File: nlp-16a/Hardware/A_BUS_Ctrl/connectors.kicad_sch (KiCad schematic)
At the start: 66 parts, among them J1 Conn_02x20_Odd_Even, J2 Conn_02x10_Counter_Clockwise, J3 Conn_02x10_Counter_Clockwise, J4 Conn_02x10_Counter_Clockwise, J5 Screw_Terminal_01x02

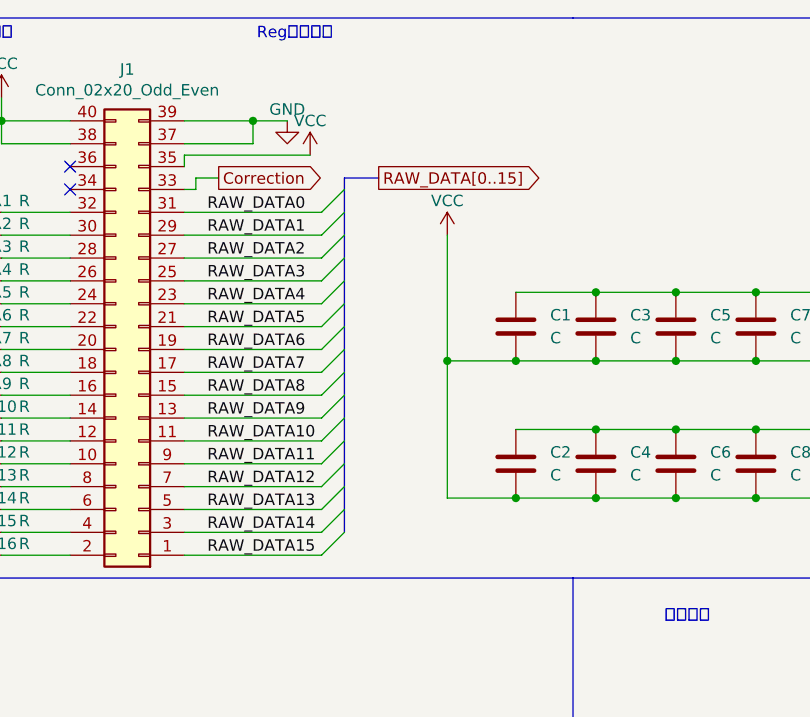
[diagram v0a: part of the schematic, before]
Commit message: テストで見つかった不具合を修正(れジスタアドレスデコーダ，Addrの内部処理の方法を変更)
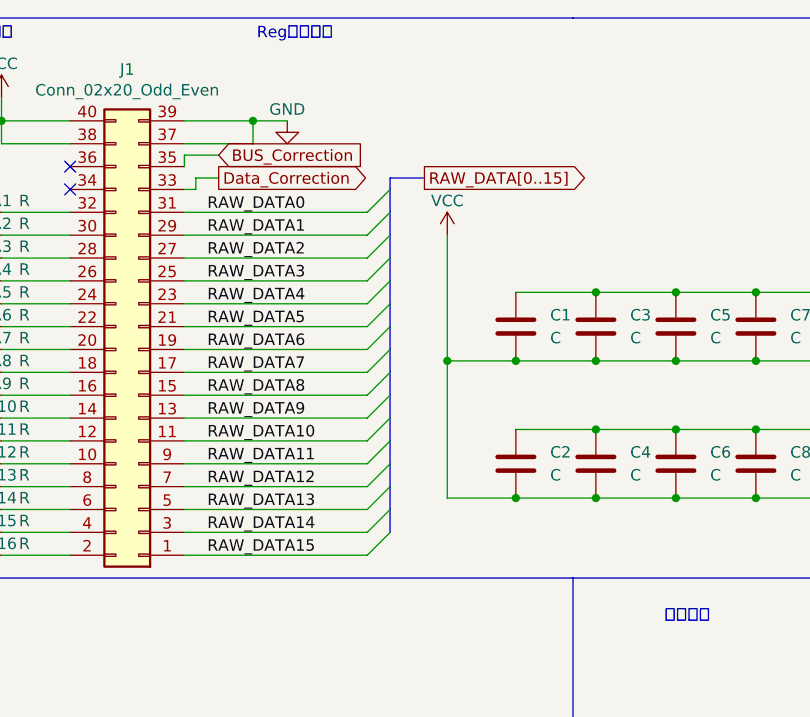
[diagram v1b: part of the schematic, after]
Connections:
- net VCC: no longer J1.35 (Pin_35)
- net Correction renamed Data_Correction
- new net BUS_Correction: J1.35 (Pin_35)

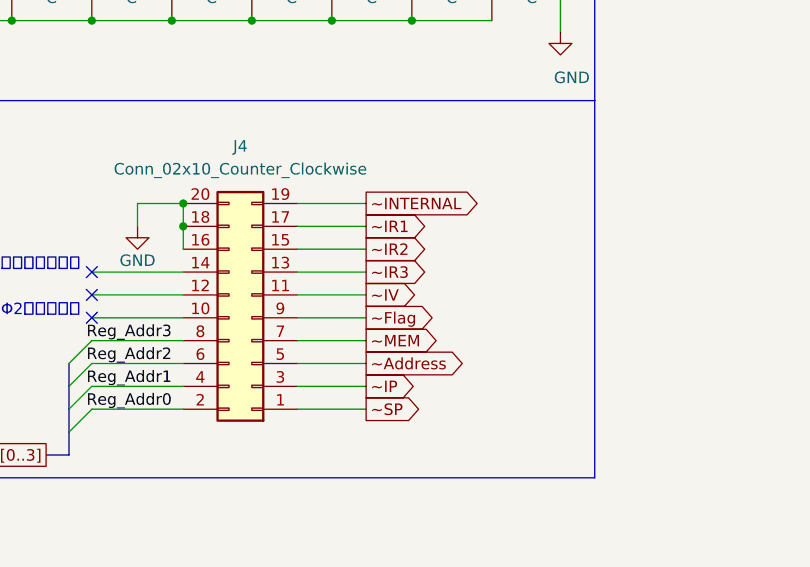
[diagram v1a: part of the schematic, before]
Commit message: A BUS制御 IVとIR3のアドレスの処理変更を反映
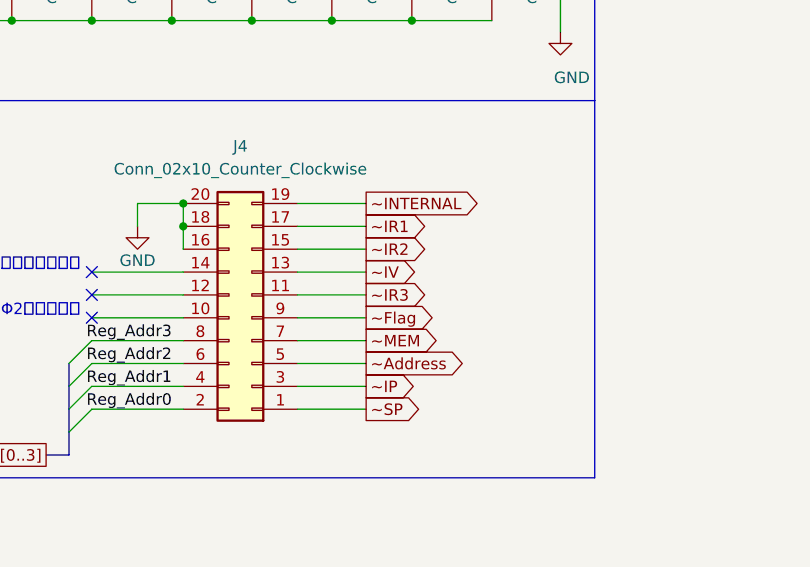
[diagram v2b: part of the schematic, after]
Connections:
- net ~IR3: now also J4.11 (Pin_11); no longer J4.13 (Pin_13)
- net ~IV: now also J4.13 (Pin_13); no longer J4.11 (Pin_11)
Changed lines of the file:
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@@
     )
   )
-  (global_label "~IV" (shape output) (at 251.46 101.6 0) (fields_autoplaced)
+  (global_label "~IV" (shape output) (at 251.46 99.06 0) (fields_autoplaced)
     (effects (font (size 1.27 1.27)) (justify left))
-    (property "Intersheet References" "${INTERSHEET_REFS}" (id 0) (at 256.4736 101.5206 0)
+    (property "Intersheet References" "${INTERSHEET_REFS}" (id 0) (at 256.4736 98.9806 0)
       (effects (font (size 1.27 1.27)) (justify left) hide)
     )
@@
     )
   )
-  (global_label "~IR3" (shape output) (at 251.46 99.06 0) (fields_autoplaced)
+  (global_label "~IR3" (shape output) (at 251.46 101.6 0) (fields_autoplaced)
     (effects (font (size 1.27 1.27)) (justify left))
-    (property "Intersheet References" "${INTERSHEET_REFS}" (id 0) (at 257.8645 98.9806 0)
+    (property "Intersheet References" "${INTERSHEET_REFS}" (id 0) (at 257.8645 101.5206 0)
       (effects (font (size 1.27 1.27)) (justify left) hide)
     )
